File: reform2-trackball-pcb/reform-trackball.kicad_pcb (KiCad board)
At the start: 2 copper layers, 83.4 x 59 mm, 42 parts, among them J1 Conn_USB, J2 Conn_01x06_Female, SW1 Choc, SW2 Choc, SW3 Choc, SW4 Choc, SW5 Choc, SW6 SW_RST, SW7 SW_HWB, U1 ATmega32U2-AU, U2 TLV75533PDBV, Y1 Crystal_GND24

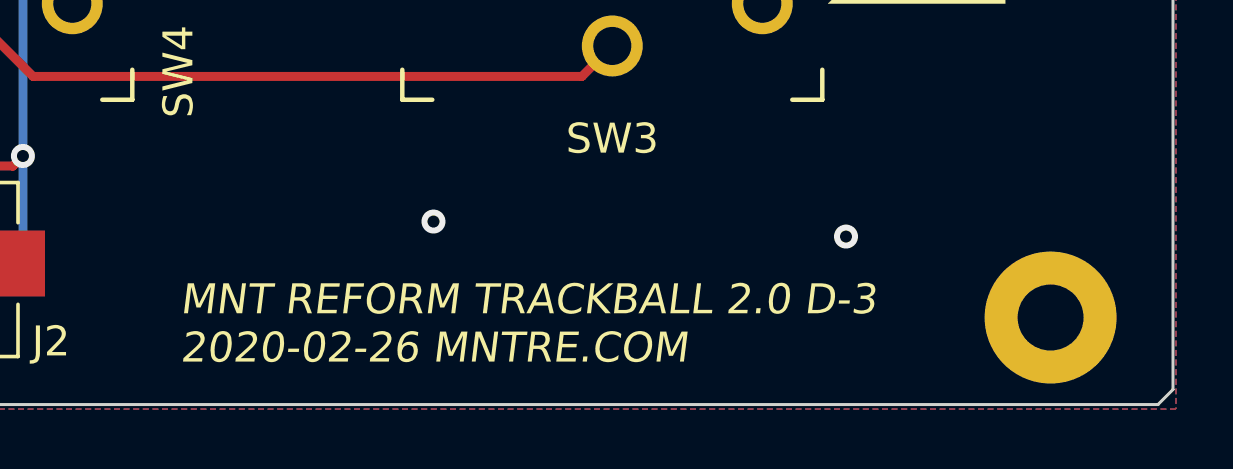
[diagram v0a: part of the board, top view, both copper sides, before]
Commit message: WIP trackball now CERN-OHL-S 2.0
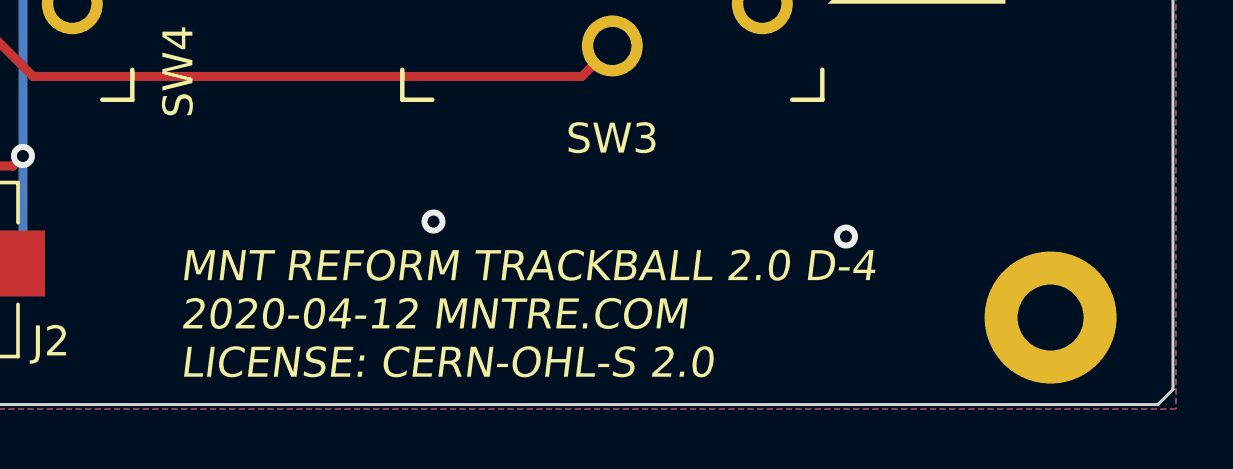
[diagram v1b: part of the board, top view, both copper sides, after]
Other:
- board text added: "MNT REFORM TRACKBALL 2.0 D-4 2020-04-12 MNTRE.COM LICENSE: CERN-OHL-S 2.0"
- board text removed: "MNT REFORM TRACKBALL 2.0 D-3 2020-02-26 MNTRE.COM"
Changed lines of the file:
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@@
     (effects (font (size 0.5 0.5) (thickness 0.1)) (justify left))
   )
-  (gr_text "MNT REFORM TRACKBALL 2.0 D-3\n2020-02-26 MNTRE.COM" (at 159.3 106.4) (layer F.SilkS)
+  (gr_text "MNT REFORM TRACKBALL 2.0 D-4\n2020-04-12 MNTRE.COM\nLICENSE: CERN-OHL-S 2.0" (at 159.3 106.1) (layer F.SilkS)
     (effects (font (size 1 1) (thickness 0.15) italic) (justify left))
   )
